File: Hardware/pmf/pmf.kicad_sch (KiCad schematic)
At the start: 4 parts, among them J1 Conn_01x06_Pin, J2 Conn_01x05_Pin, J3 Conn_01x06_Socket, J4 Conn_01x05_Socket

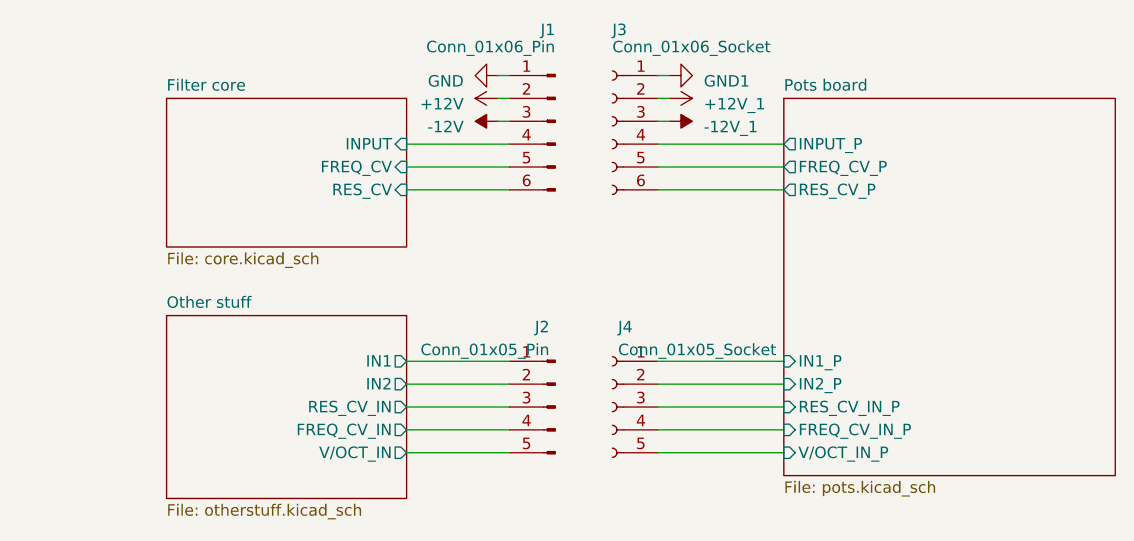
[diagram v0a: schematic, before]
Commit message: Global labels to heir, fixing input bug; buffer LP1-4; more clearance for rot switch
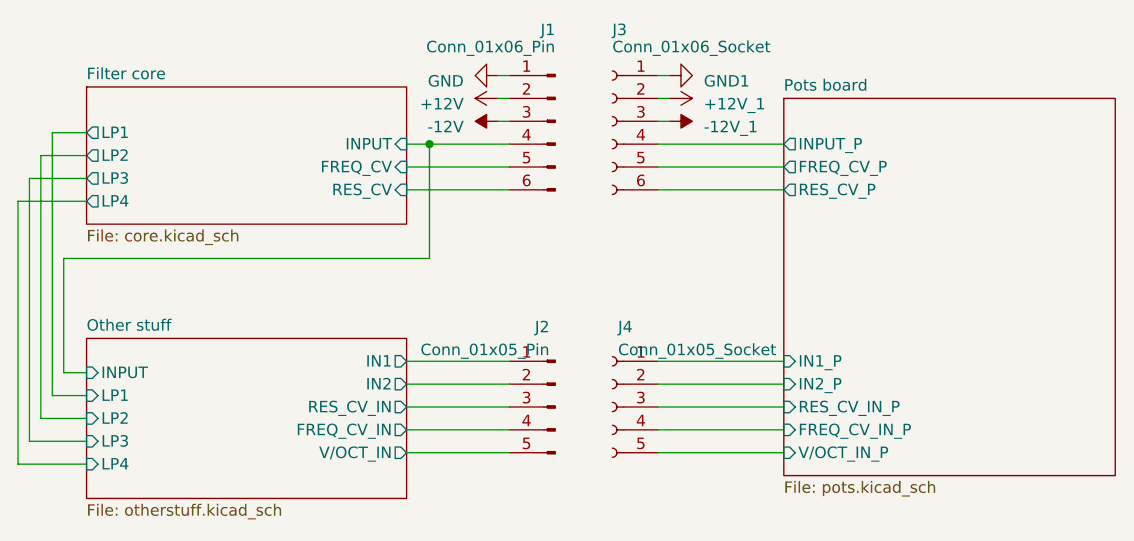
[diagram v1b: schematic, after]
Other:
- sheet Filter core ports: added LP1, LP2, LP3, LP4; removed none
- sheet Other stuff ports: added INPUT, LP1, LP2, LP3, LP4; removed none
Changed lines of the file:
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@@
     (comment 3 "Based on Electric Druid design ")
   )
+  (junction (at 114.3 72.39) (diameter 0) (color 0 0 0 0)
+  )
+  (wire (pts (xy 76.2 73.66) (xy 71.12 73.66))
+    (stroke (width 0) (type default))
+  )
   (wire (pts (xy 111.76 74.93) (xy 123.19 74.93))
     (stroke (width 0) (type default))
   )
+  (wire (pts (xy 68.58 78.74) (xy 68.58 107.95))
+    (stroke (width 0) (type default))
+  )
   (wire (pts (xy 139.7 72.39) (xy 153.67 72.39))
     (stroke (width 0) (type default))
   )
+  (wire (pts (xy 72.39 100.33) (xy 76.2 100.33))
+    (stroke (width 0) (type default))
+  )
   (wire (pts (xy 121.92 64.77) (xy 123.19 64.77))
     (stroke (width 0) (type default))
@@
     (stroke (width 0) (type default))
   )
+  (wire (pts (xy 76.2 71.12) (xy 72.39 71.12))
+    (stroke (width 0) (type default))
+  )
   (wire (pts (xy 139.7 104.14) (xy 153.67 104.14))
     (stroke (width 0) (type default))
   )
+  (wire (pts (xy 114.3 72.39) (xy 123.19 72.39))
+    (stroke (width 0) (type default))
+  )
+  (wire (pts (xy 114.3 85.09) (xy 73.66 85.09))
+    (stroke (width 0) (type default))
+  )
+  (wire (pts (xy 69.85 105.41) (xy 76.2 105.41))
+    (stroke (width 0) (type default))
+  )
+  (wire (pts (xy 73.66 85.09) (xy 73.66 97.79))
+    (stroke (width 0) (type default))
+  )
   (wire (pts (xy 139.7 96.52) (xy 153.67 96.52))
     (stroke (width 0) (type default))
@@
     (stroke (width 0) (type default))
   )
+  (wire (pts (xy 76.2 76.2) (xy 69.85 76.2))
+    (stroke (width 0) (type default))
+  )
   (wire (pts (xy 111.76 96.52) (xy 123.19 96.52))
     (stroke (width 0) (type default))
   )
+  (wire (pts (xy 69.85 76.2) (xy 69.85 105.41))
+    (stroke (width 0) (type default))
+  )
+  (wire (pts (xy 72.39 71.12) (xy 72.39 100.33))
+    (stroke (width 0) (type default))
+  )
   (wire (pts (xy 139.7 101.6) (xy 153.67 101.6))
     (stroke (width 0) (type default))
   )
+  (wire (pts (xy 71.12 73.66) (xy 71.12 102.87))
+    (stroke (width 0) (type default))
+  )
   (wire (pts (xy 139.7 64.77) (xy 140.97 64.77))
     (stroke (width 0) (type default))
@@
     (stroke (width 0) (type default))
   )
-  (wire (pts (xy 111.76 72.39) (xy 123.19 72.39))
+  (wire (pts (xy 71.12 102.87) (xy 76.2 102.87))
+    (stroke (width 0) (type default))
+  )
+  (wire (pts (xy 111.76 72.39) (xy 114.3 72.39))
     (stroke (width 0) (type default))
   )
@@
     (stroke (width 0) (type default))
   )
+  (wire (pts (xy 114.3 72.39) (xy 114.3 85.09))
+    (stroke (width 0) (type default))
+  )
+  (wire (pts (xy 68.58 107.95) (xy 76.2 107.95))
+    (stroke (width 0) (type default))
+  )
   (wire (pts (xy 139.7 69.85) (xy 140.97 69.85))
     (stroke (width 0) (type default))
   )
+  (wire (pts (xy 73.66 97.79) (xy 76.2 97.79))
+    (stroke (width 0) (type default))
+  )
   (wire (pts (xy 111.76 106.68) (xy 123.19 106.68))
+    (stroke (width 0) (type default))
+  )
+  (wire (pts (xy 76.2 78.74) (xy 68.58 78.74))
     (stroke (width 0) (type default))
   )
@@
     )
   )
-  (sheet (at 85.09 67.31) (size 26.67 16.51) (fields_autoplaced)
+  (sheet (at 76.2 66.04) (size 35.56 15.24) (fields_autoplaced)
     (stroke (width 0.1524) (type solid))
     (fill (color 0 0 0 0.0000))
-    (property "Sheetname" "Filter core" (at 85.09 66.5984 0)
+    (property "Sheetname" "Filter core" (at 76.2 65.3284 0)
       (effects (font (size 1.27 1.27)) (justify left bottom))
     )
-    (property "Sheetfile" "core.kicad_sch" (at 85.09 84.4046 0)
+    (property "Sheetfile" "core.kicad_sch" (at 76.2 81.8646 0)
       (effects (font (size 1.27 1.27)) (justify left top))
     )
@@
       (effects (font (size 1.27 1.27)) (justify right))
     )
+    (pin "LP3" output (at 76.2 76.2 180)
+      (effects (font (size 1.27 1.27)) (justify left))
+    )
+    (pin "LP4" output (at 76.2 78.74 180)
+      (effects (font (size 1.27 1.27)) (justify left))
+    )
+    (pin "LP2" output (at 76.2 73.66 180)
+      (effects (font (size 1.27 1.27)) (justify left))
+    )
+    (pin "LP1" output (at 76.2 71.12 180)
+      (effects (font (size 1.27 1.27)) (justify left))
+    )
     (instances
       (project "pmf"
@@
     )
   )
-  (sheet (at 85.09 91.44) (size 26.67 20.32) (fields_autoplaced)
+  (sheet (at 76.2 93.98) (size 35.56 17.78) (fields_autoplaced)
     (stroke (width 0.1524) (type solid))
     (fill (color 0 0 0 0.0000))
-    (property "Sheetname" "Other stuff" (at 85.09 90.7284 0)
+    (property "Sheetname" "Other stuff" (at 76.2 93.2684 0)
       (effects (font (size 1.27 1.27)) (justify left bottom))
     )
-    (property "Sheetfile" "otherstuff.kicad_sch" (at 85.09 112.3446 0)
+    (property "Sheetfile" "otherstuff.kicad_sch" (at 76.2 112.3446 0)
       (effects (font (size 1.27 1.27)) (justify left top))
     )
@@
       (effects (font (size 1.27 1.27)) (justify right))
     )
-    (instances
+    (pin "LP2" input (at 76.2 102.87 180)
+      (effects (font (size 1.27 1.27)) (justify left))
+    )
+    (pin "LP1" input (at 76.2 100.33 180)
+      (effects (font (size 1.27 1.27)) (justify left))
+    )
+    (pin "LP3" input (at 76.2 105.41 180)
+      (effects (font (size 1.27 1.27)) (justify left))
+    )
+    (pin "LP4" input (at 76.2 107.95 180)
+      (effects (font (size 1.27 1.27)) (justify left))
+    )
+    (pin "INPUT" input (at 76.2 97.79 180)
+      (effects (font (size 1.27 1.27)) (justify left))
+    )
+    (instances
